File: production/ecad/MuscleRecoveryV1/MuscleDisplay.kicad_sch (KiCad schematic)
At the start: 18 parts, among them J3 Motor_Screw_Terminal, J7 Conn_01x11_Pin, Q4 AO3400A

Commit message: updated footprints and emg schematic
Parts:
- J3: footprint (none) -> Connector_PinHeader_2.54mm:PinHeader_1x02_P2.54mm_Horizontal
- J7: footprint (none) -> Connector_PinHeader_2.54mm:PinHeader_1x11_P2.54mm_Horizontal
- R35, R50, R51, R52, R53, R54, R55, R56, R57, R58, R59, R60: footprint (none) -> Resistor_SMD:R_0805_2012Metric
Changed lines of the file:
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@@
       (effects (font (size 1.27 1.27)))
     )
-    (property "Footprint" "" (at 123.19 41.91 0)
+    (property "Footprint" "Resistor_SMD:R_0805_2012Metric" (at 123.19 41.91 0)
       (effects (font (size 1.27 1.27)) hide)
     )
@@
       (effects (font (size 1.27 1.27)))
     )
-    (property "Footprint" "" (at 123.19 59.69 0)
+    (property "Footprint" "Resistor_SMD:R_0805_2012Metric" (at 123.19 59.69 0)
       (effects (font (size 1.27 1.27)) hide)
     )
@@
       (effects (font (size 1.27 1.27)))
     )
-    (property "Footprint" "" (at 123.19 52.07 0)
+    (property "Footprint" "Resistor_SMD:R_0805_2012Metric" (at 123.19 52.07 0)
       (effects (font (size 1.27 1.27)) hide)
     )
@@
       (effects (font (size 1.27 1.27)))
     )
-    (property "Footprint" "" (at 123.19 49.53 0)
+    (property "Footprint" "Resistor_SMD:R_0805_2012Metric" (at 123.19 49.53 0)
       (effects (font (size 1.27 1.27)) hide)
     )
@@
       (effects (font (size 1.27 1.27)) (justify left))
     )
-    (property "Footprint" "" (at 172.72 95.25 0)
+    (property "Footprint" "Connector_PinHeader_2.54mm:PinHeader_1x02_P2.54mm_Horizontal" (at 172.72 95.25 0)
       (effects (font (size 1.27 1.27)) hide)
     )
@@
       (effects (font (size 1.27 1.27)))
     )
-    (property "Footprint" "" (at 123.19 54.61 0)
+    (property "Footprint" "Resistor_SMD:R_0805_2012Metric" (at 123.19 54.61 0)
       (effects (font (size 1.27 1.27)) hide)
     )
@@
       (effects (font (size 1.27 1.27)))
     )
-    (property "Footprint" "" (at 123.19 44.45 0)
+    (property "Footprint" "Resistor_SMD:R_0805_2012Metric" (at 123.19 44.45 0)
       (effects (font (size 1.27 1.27)) hide)
     )
@@
       (effects (font (size 1.27 1.27)))
     )
-    (property "Footprint" "" (at 137.16 46.99 0)
+    (property "Footprint" "Connector_PinHeader_2.54mm:PinHeader_1x11_P2.54mm_Horizontal" (at 137.16 46.99 0)
       (effects (font (size 1.27 1.27)) hide)
     )
@@
       (effects (font (size 1.27 1.27)) (justify left))
     )
-    (property "Footprint" "" (at 60.96 137.16 0)
+    (property "Footprint" "Resistor_SMD:R_0805_2012Metric" (at 60.96 137.16 0)
       (effects (font (size 1.27 1.27)) hide)
     )
@@
       (effects (font (size 1.27 1.27)) (justify left))
     )
-    (property "Footprint" "" (at 60.96 92.71 0)
+    (property "Footprint" "Resistor_SMD:R_0805_2012Metric" (at 60.96 92.71 0)
       (effects (font (size 1.27 1.27)) hide)
     )
@@
       (effects (font (size 1.27 1.27)))
     )
-    (property "Footprint" "" (at 123.19 46.99 0)
+    (property "Footprint" "Resistor_SMD:R_0805_2012Metric" (at 123.19 46.99 0)
       (effects (font (size 1.27 1.27)) hide)
     )
@@
       (effects (font (size 1.27 1.27)))
     )
-    (property "Footprint" "" (at 149.86 113.03 0)
+    (property "Footprint" "Resistor_SMD:R_0805_2012Metric" (at 149.86 113.03 0)
       (effects (font (size 1.27 1.27)) hide)
     )
@@
       (effects (font (size 1.27 1.27)))
     )
-    (property "Footprint" "" (at 123.19 57.15 0)
+    (property "Footprint" "Resistor_SMD:R_0805_2012Metric" (at 123.19 57.15 0)
       (effects (font (size 1.27 1.27)) hide)
     )
@@
       (effects (font (size 1.27 1.27)) (justify left))
     )
-    (property "Footprint" "" (at 158.75 118.11 0)
-      (effects (font (size 1.27 1.27)) hide)
-    )
+    (property "Footprint" "Resistor_SMD:R_0805_2012Metric" (at 158.75 118.11 0)
+      (effects (font (size 1.27 1.27)) hide)
+    )

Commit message: updated footprint assignments for ESP32 and S1-S4 to reference the folder Andy made
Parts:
- S1, S4: footprint B3F-1000:SW_B3F-1000 -> Muscle_Recovery_Footprint_Library:SW_B3F-1000
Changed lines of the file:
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@@
       (effects (font (size 1.27 1.27)))
     )
-    (property "Footprint" "B3F-1000:SW_B3F-1000" (at 76.2 109.22 0)
+    (property "Footprint" "Muscle_Recovery_Footprint_Library:SW_B3F-1000" (at 76.2 109.22 0)
       (effects (font (size 1.27 1.27)) (justify bottom) hide)
     )
@@
       (effects (font (size 1.27 1.27)))
     )
-    (property "Footprint" "B3F-1000:SW_B3F-1000" (at 76.2 153.67 0)
+    (property "Footprint" "Muscle_Recovery_Footprint_Library:SW_B3F-1000" (at 76.2 153.67 0)
       (effects (font (size 1.27 1.27)) (justify bottom) hide)
     )

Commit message: supposedly finished schematic and footprints and started PCB
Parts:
- J3: footprint Connector_PinHeader_2.54mm:PinHeader_1x02_P2.54mm_Horizontal -> Connector_PinHeader_2.54mm:PinHeader_1x02_P2.54mm_Vertical
- J7: footprint Connector_PinHeader_2.54mm:PinHeader_1x11_P2.54mm_Horizontal -> Connector_PinHeader_2.54mm:PinHeader_1x11_P2.54mm_Vertical
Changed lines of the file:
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@@
       (effects (font (size 1.27 1.27)) (justify left))
     )
-    (property "Footprint" "Connector_PinHeader_2.54mm:PinHeader_1x02_P2.54mm_Horizontal" (at 172.72 95.25 0)
+    (property "Footprint" "Connector_PinHeader_2.54mm:PinHeader_1x02_P2.54mm_Vertical" (at 172.72 95.25 0)
       (effects (font (size 1.27 1.27)) hide)
     )
@@
       (effects (font (size 1.27 1.27)))
     )
-    (property "Footprint" "Connector_PinHeader_2.54mm:PinHeader_1x11_P2.54mm_Horizontal" (at 137.16 46.99 0)
+    (property "Footprint" "Connector_PinHeader_2.54mm:PinHeader_1x11_P2.54mm_Vertical" (at 137.16 46.99 0)
       (effects (font (size 1.27 1.27)) hide)
     )

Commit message: pushing current layout and other changes to be able to pull
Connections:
- net +3.3V renamed +3V3

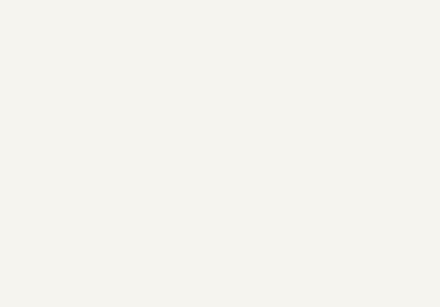
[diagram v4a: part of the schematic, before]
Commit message: added accelerometer
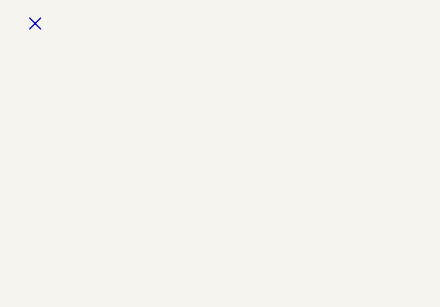
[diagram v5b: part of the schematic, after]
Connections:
- no-connect marks 5 -> 6
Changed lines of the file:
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@@
   (no_connect (at 80.01 133.35))
   (no_connect (at 80.01 85.09))
+  (no_connect (at 36.83 11.43))
   (no_connect (at 132.08 34.29))
   (no_connect (at 80.01 129.54))
@@
   (symbol (lib_id "power:+3V3") (at 172.72 85.09 0) (unit 1)
     (in_bom yes) (on_board yes) (dnp no) (fields_autoplaced)
-    (property "Reference" "#PWR065" (at 172.72 88.9 0)
+    (property "Reference" "#PWR071" (at 172.72 88.9 0)
       (effects (font (size 1.27 1.27)) hide)
     )
@@
     (instances
       (project "MuscleRecoveryV1"
-        (path "/4e550305-79d2-4e4a-a502-817ebcc79f9a"
-          (reference "#PWR065") (unit 1)
-        )
         (path "/4e550305-79d2-4e4a-a502-817ebcc79f9a/85edd68f-6119-4dbf-9af0-99f996378c09"
           (reference "#PWR071") (unit 1)
@@
   (symbol (lib_id "power:+3V3") (at 100.33 34.29 0) (unit 1)
     (in_bom yes) (on_board yes) (dnp no) (fields_autoplaced)
-    (property "Reference" "#PWR065" (at 100.33 38.1 0)
+    (property "Reference" "#PWR055" (at 100.33 38.1 0)
       (effects (font (size 1.27 1.27)) hide)
     )
@@
     (instances
       (project "MuscleRecoveryV1"
-        (path "/4e550305-79d2-4e4a-a502-817ebcc79f9a"
-          (reference "#PWR065") (unit 1)
-        )
         (path "/4e550305-79d2-4e4a-a502-817ebcc79f9a/85edd68f-6119-4dbf-9af0-99f996378c09"
           (reference "#PWR055") (unit 1)
@@
   (symbol (lib_id "power:+3V3") (at 52.07 124.46 0) (unit 1)
     (in_bom yes) (on_board yes) (dnp no) (fields_autoplaced)
-    (property "Reference" "#PWR065" (at 52.07 128.27 0)
+    (property "Reference" "#PWR061" (at 52.07 128.27 0)
       (effects (font (size 1.27 1.27)) hide)
     )
@@
     (instances
       (project "MuscleRecoveryV1"
-        (path "/4e550305-79d2-4e4a-a502-817ebcc79f9a"
-          (reference "#PWR065") (unit 1)
-        )
         (path "/4e550305-79d2-4e4a-a502-817ebcc79f9a/85edd68f-6119-4dbf-9af0-99f996378c09"
           (reference "#PWR061") (unit 1)
@@
   (symbol (lib_id "power:+3V3") (at 52.07 82.55 0) (unit 1)
     (in_bom yes) (on_board yes) (dnp no) (fields_autoplaced)
-    (property "Reference" "#PWR065" (at 52.07 86.36 0)
+    (property "Reference" "#PWR053" (at 52.07 86.36 0)
       (effects (font (size 1.27 1.27)) hide)
     )
@@
     (instances
       (project "MuscleRecoveryV1"
-        (path "/4e550305-79d2-4e4a-a502-817ebcc79f9a"
-          (reference "#PWR065") (unit 1)
-        )
         (path "/4e550305-79d2-4e4a-a502-817ebcc79f9a/85edd68f-6119-4dbf-9af0-99f996378c09"
           (reference "#PWR053") (unit 1)
